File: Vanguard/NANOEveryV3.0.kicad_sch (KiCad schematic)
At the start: 57 parts, among them IC1 MPM3610, J1 -, J2 DNP, Q1 BSS138PS, Q2 BSS138PS, U1 ATMEGA4809, U2 AP2112K-3.3, U3 ATSAMD11D14A, U4 ICM-20602, U5 LM34DM_NOPB

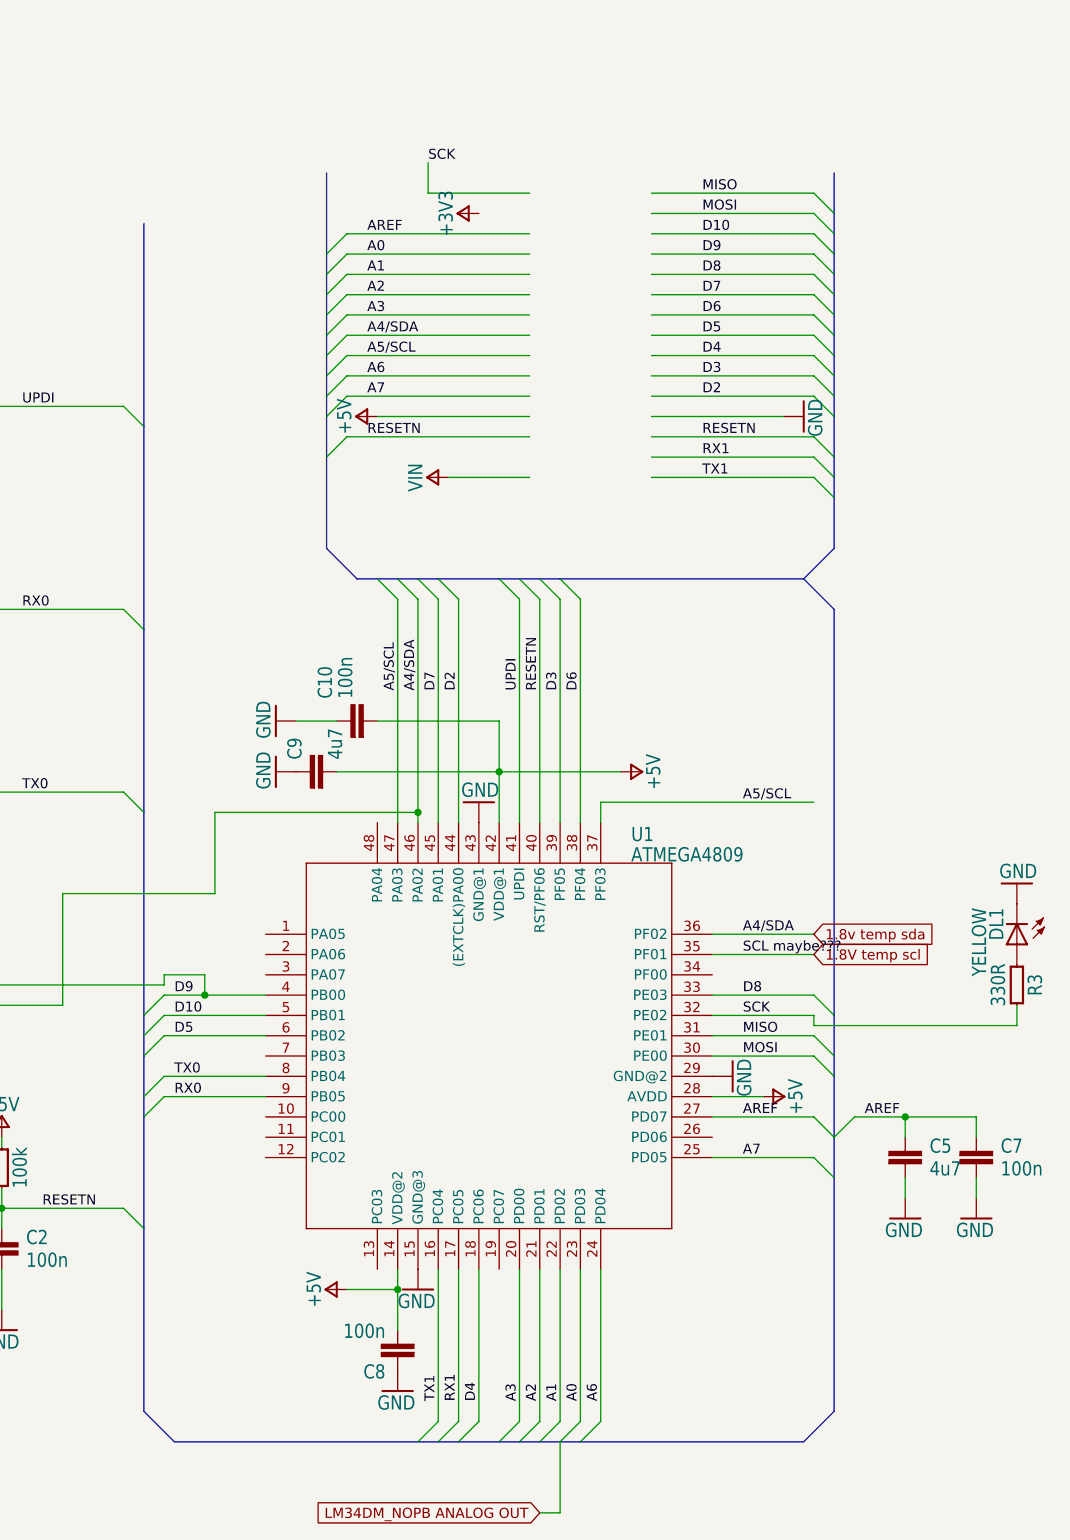
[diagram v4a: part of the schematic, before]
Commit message: removed headers + added mcu
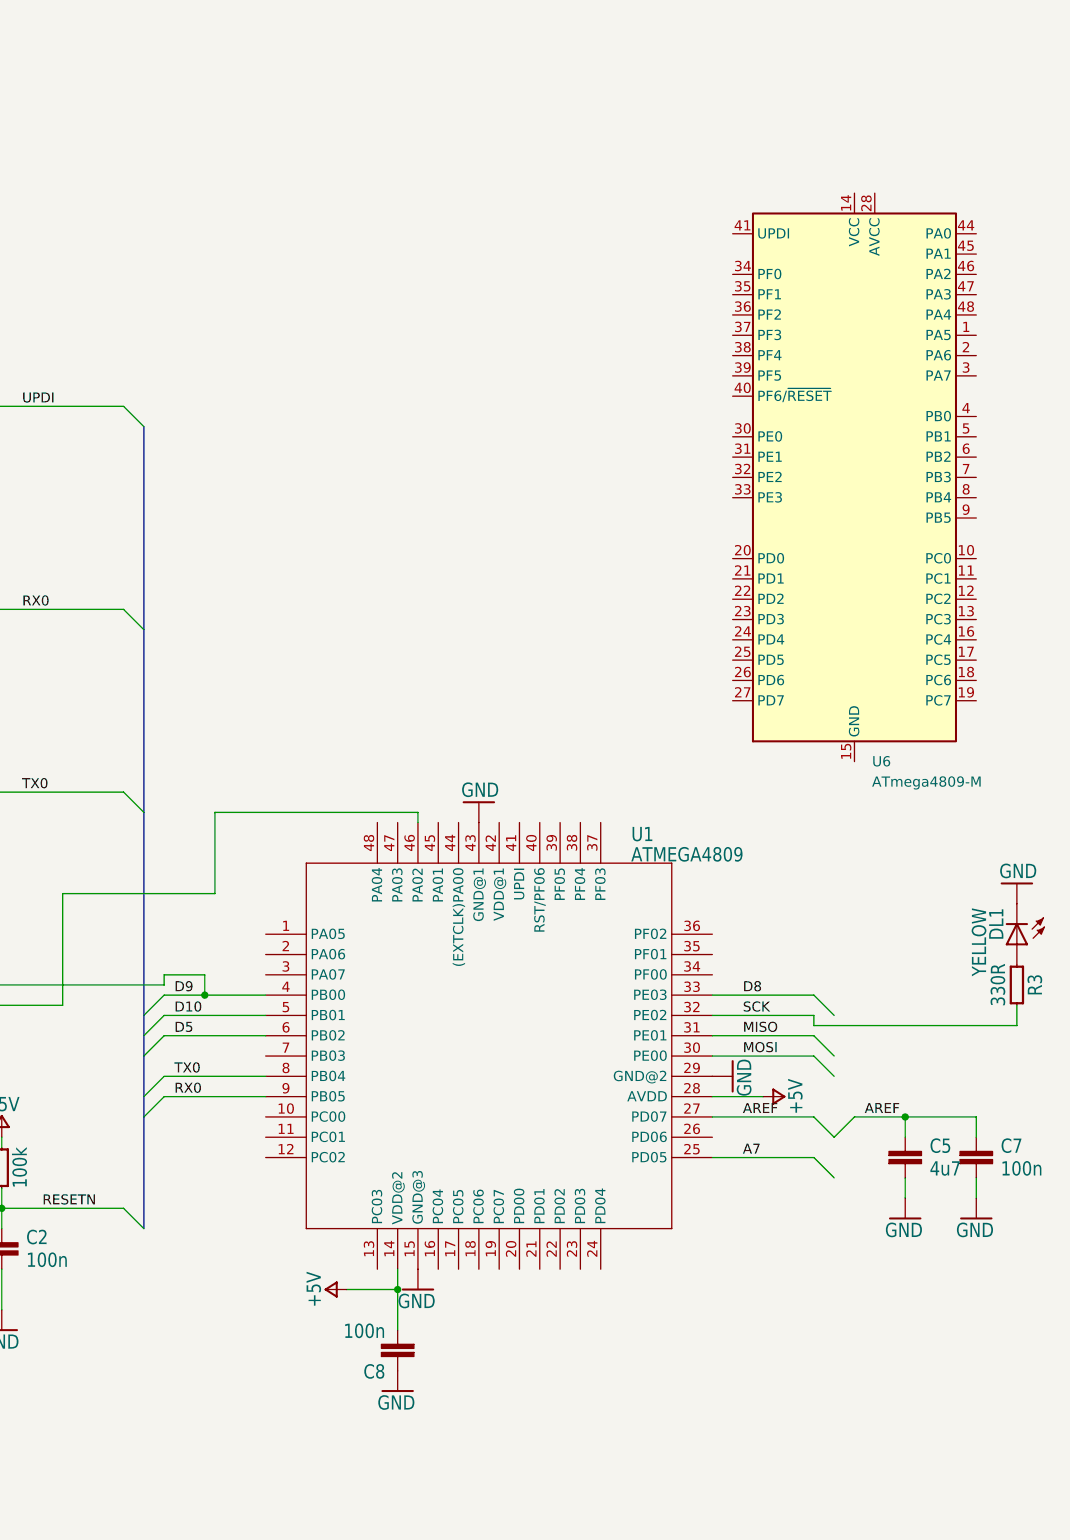
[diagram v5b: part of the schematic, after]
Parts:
- removed C10: 100n, Capacitor_SMD:C_0402_1005Metric, symbol NANOEveryV3.0-eagle-import:C-0402
- removed C9: 4u7, Capacitor_SMD:C_0402_1005Metric, symbol NANOEveryV3.0-eagle-import:C-0402
- added U6: ATmega4809-M, Package_DFN_QFN:UQFN-48-1EP_6x6mm_P0.4mm_EP4.62x4.62mm, symbol MCU_Microchip_ATmega:ATmega4809-M
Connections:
- net +5V: no longer U1.42 (VDD@1)
- net RESETN: no longer U1.40 (RST/PF06)
- net UPDI: no longer U1.41 (UPDI)
- net 1.8V temp scl: no longer names the net of U1.35 (PF01)
- net 1.8v temp sda: no longer names the net of U1.46 (PA02), U4.3 (SDA/SDI)
- net 1.8v temp sda: no longer U1.36 (PF02)
- net A0: no longer names the net of U1.23 (PD03)
- net A1: no longer names the net of U1.22 (PD02)
- net A2: no longer names the net of U1.21 (PD01)
- net A3: no longer names the net of U1.20 (PD00)
- net A5/SCL: no longer names the net of U1.37 (PF03)
- net A5/SCL: no longer U1.47 (PA03)
- net A6: no longer names the net of U1.24 (PD04)
- net D2: no longer names the net of U1.44 ((EXTCLK)PA00)
- net D3~{}: no longer names the net of U1.39 (PF05)
- net D4: no longer names the net of U1.18 (PC06)
- net D6~{}: no longer names the net of U1.38 (PF04)
- net D7: no longer names the net of U1.45 (PA01)
- net RX1: no longer names the net of U1.17 (PC05)
- net TX1: no longer names the net of U1.16 (PC04)
- new net: U6.14 (VCC), U6.42 (VCC)
- new net: U6.15 (GND), U6.29 (GND), U6.43 (GND), U6.49 (GND)

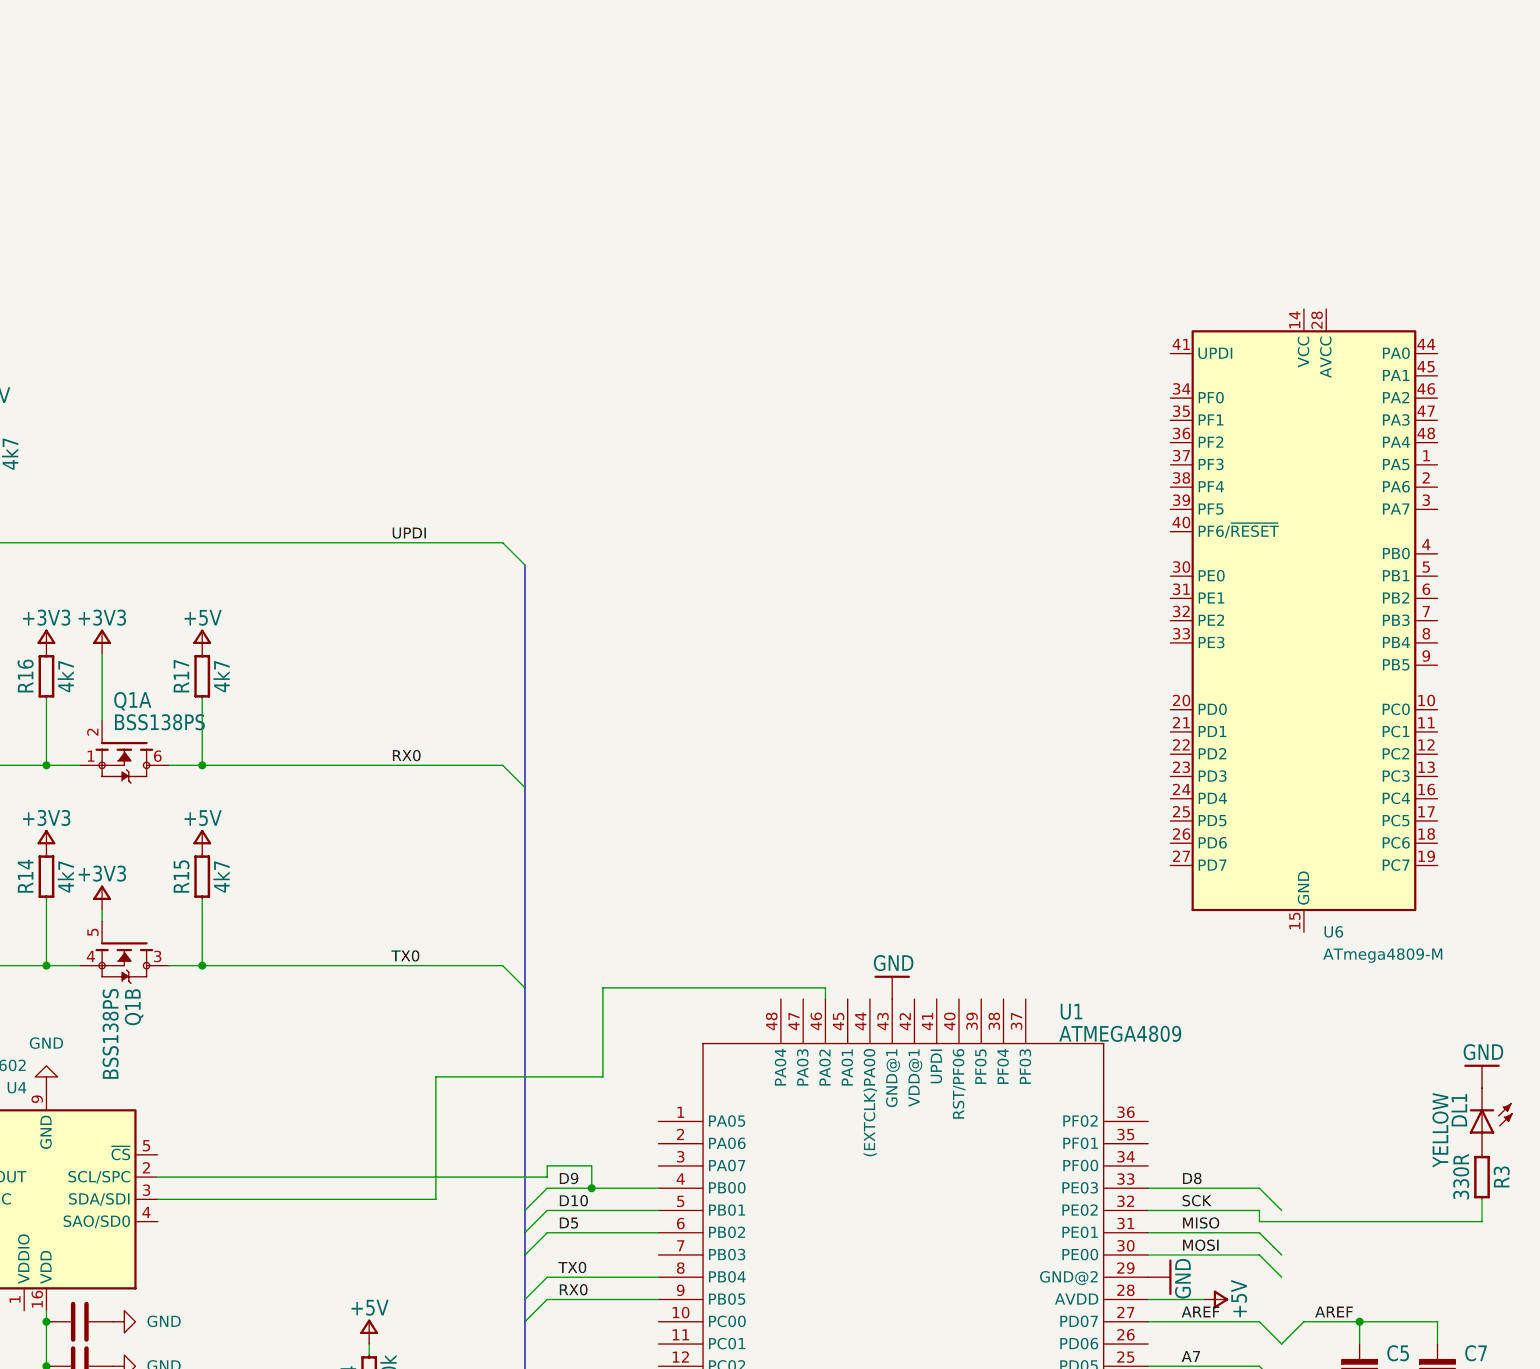
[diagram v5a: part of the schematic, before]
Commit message: New atmega chip added basic rewiring
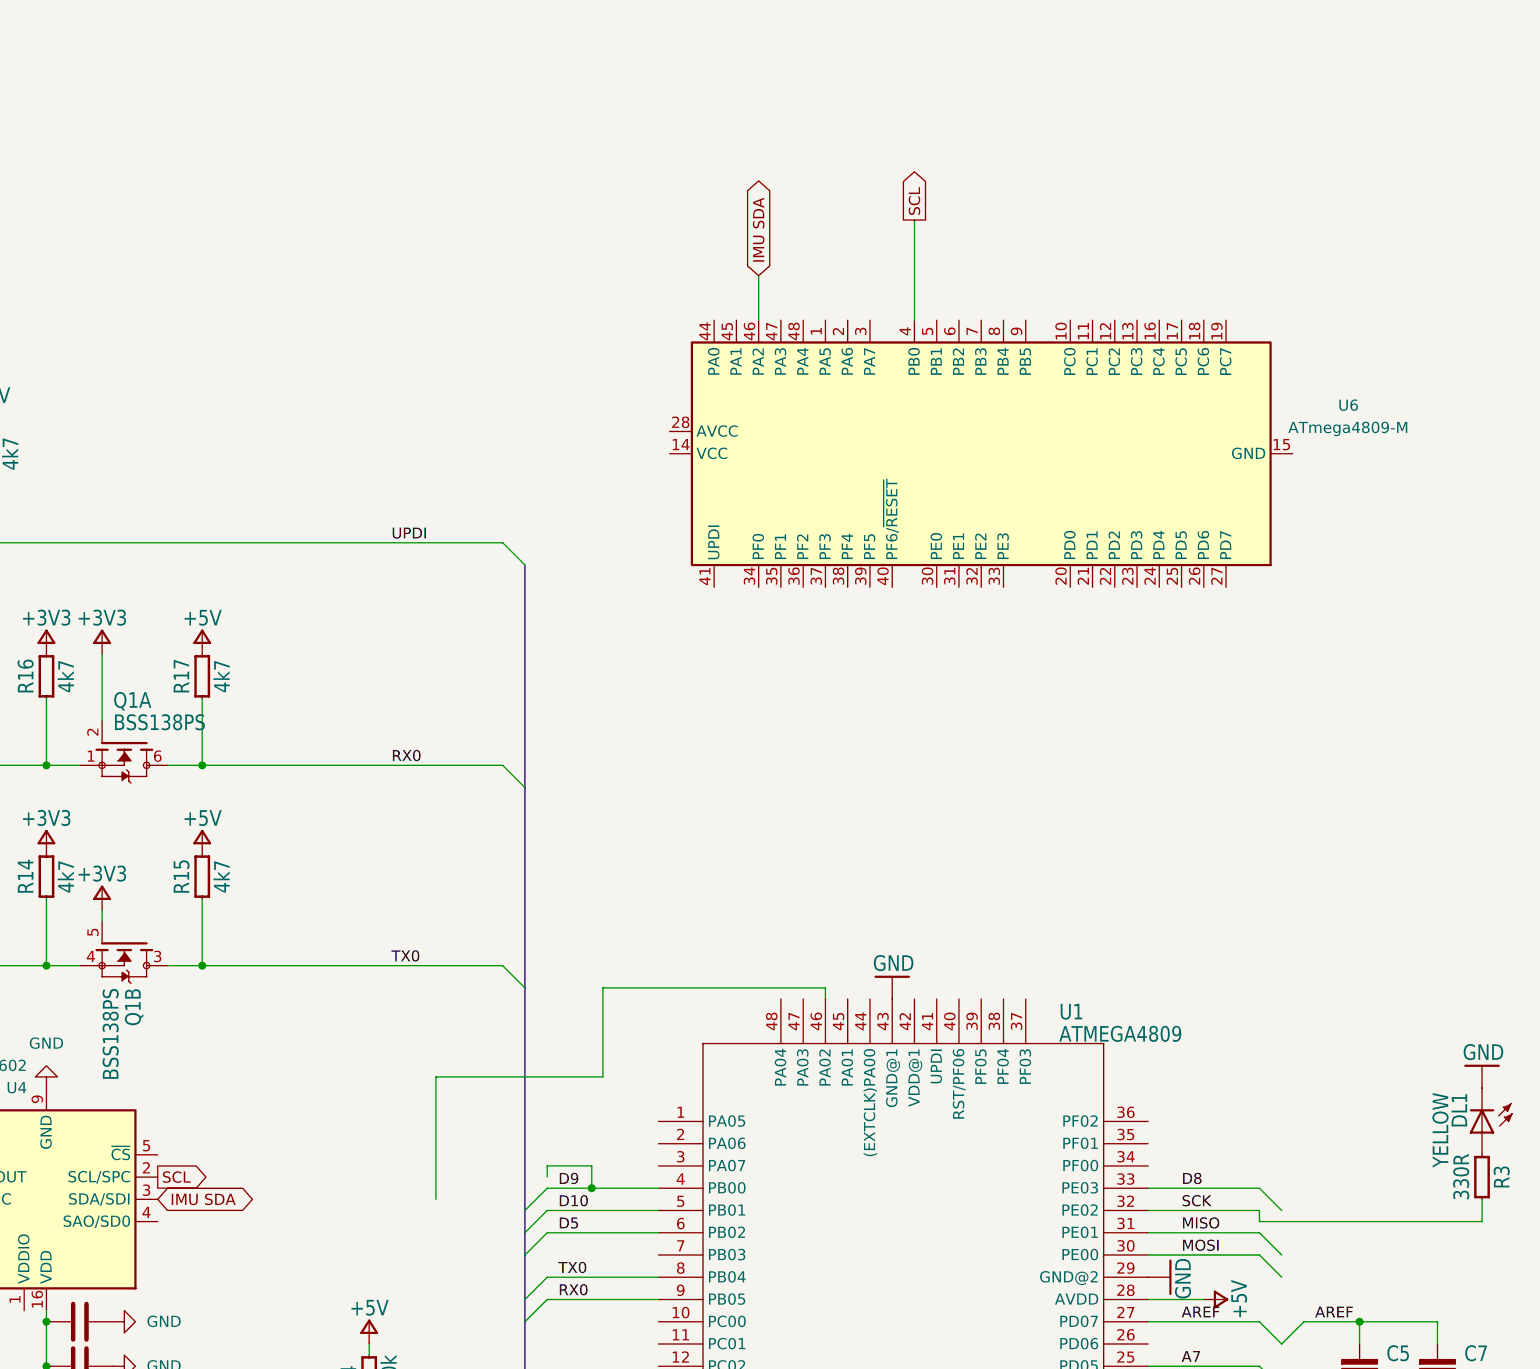
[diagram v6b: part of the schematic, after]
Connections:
- net D9~{}: no longer U4.2 (SCL/SPC)
- net at U1.46 (PA02): no longer U4.3 (SDA/SDI)
- net SCL: now reaches U6.4 (PB0)
- net SCL: now also U4.2 (SCL/SPC)
- net IMU SDA: now reaches U6.46 (PA2)
- net IMU SDA: now also U4.3 (SDA/SDI)
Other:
- moved on the sheet: U6
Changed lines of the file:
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@@
 	(wire
 		(pts
+			(xy 311.15 71.12) (xy 311.15 82.55)
+		)
+		(stroke
+			(width 0)
+			(type default)
+		)
+	)
+	(wire
+		(pts
 			(xy 73.66 50.8) (xy 73.66 52.07)
 		)
@@
 	(wire
 		(pts
-			(xy 111.76 50.8) (xy 111.76 49.53)
+			(xy 293.37 77.47) (xy 293.37 82.55)
 		)
 		(stroke
-			(width 0.1524)
-			(type solid)
+			(width 0)
+			(type default)
 		)
 	)
 	(wire
 		(pts
-			(xy 138.43 135.89) (xy 166.37 135.89)
+			(xy 111.76 50.8) (xy 111.76 49.53)
 		)
 		(stroke
@@
 	(wire
 		(pts
-			(xy 194.31 114.3) (xy 187.96 114.3)
+			(xy 138.43 135.89) (xy 166.37 135.89)
 		)
 		(stroke
@@
 	(wire
 		(pts
-			(xy 224.79 182.88) (xy 256.54 182.88)
+			(xy 194.31 114.3) (xy 187.96 114.3)
 		)
 		(stroke
-			(width 0)
-			(type default)
+			(width 0.1524)
+			(type solid)
 		)
 	)
@@
 	(wire
 		(pts
-			(xy 224.79 180.34) (xy 269.24 180.34)
-		)
-		(stroke
-			(width 0)
-			(type default)
-		)
-	)
-	(wire
-		(pts
 			(xy 186.69 123.19) (xy 186.69 125.73)
 		)
@@
 		)
 	)
+	(global_label "SCL"
+		(shape output)
+		(at 311.15 71.12 90)
+		(fields_autoplaced yes)
+		(effects
+			(font
+				(size 1.27 1.27)
+			)
+			(justify left)
+		)
+		(property "Intersheetrefs" "${INTERSHEET_REFS}"
+			(at 311.15 64.6272 90)
+			(effects
+				(font
+					(size 1.27 1.27)
+				)
+				(justify left)
+				(hide yes)
+			)
+		)
+	)
+	(global_label "IMU SDA"
+		(shape bidirectional)
+		(at 293.37 77.47 90)
+		(fields_autoplaced yes)
+		(effects
+			(font
+				(size 1.27 1.27)
+			)
+			(justify left)
+		)
+		(property "Intersheetrefs" "${INTERSHEET_REFS}"
+			(at 293.37 65.4511 90)
+			(effects
+				(font
+					(size 1.27 1.27)
+				)
+				(justify left)
+				(hide yes)
+			)
+		)
+	)
+	(global_label "SCL"
+		(shape output)
+		(at 224.79 180.34 0)
+		(fields_autoplaced yes)
+		(effects
+			(font
+				(size 1.27 1.27)
+			)
+			(justify left)
+		)
+		(property "Intersheetrefs" "${INTERSHEET_REFS}"
+			(at 231.2828 180.34 0)
+			(effects
+				(font
+					(size 1.27 1.27)
+				)
+				(justify left)
+				(hide yes)
+			)
+		)
+	)
 	(global_label "LM34DM_NOPB ANALOG OUT"
 		(shape input)
@@
 		)
 	)
+	(global_label "IMU SDA"
+		(shape bidirectional)
+		(at 224.79 182.88 0)
+		(fields_autoplaced yes)
+		(effects
+			(font
+				(size 1.27 1.27)
+			)
+			(justify left)
+		)
+		(property "Intersheetrefs" "${INTERSHEET_REFS}"
+			(at 236.8089 182.88 0)
+			(effects
+				(font
+					(size 1.27 1.27)
+				)
+				(justify left)
+				(hide yes)
+			)
+		)
+	)
 	(symbol
 		(lib_id "NANOEveryV3.0-eagle-import:Arduino-supply_GND")
@@
 	(symbol
 		(lib_id "MCU_Microchip_ATmega:ATmega4809-M")
-		(at 355.6 116.84 0)
+		(at 318.77 97.79 90)
 		(unit 1)
 		(exclude_from_sim no)
@@
 		(fields_autoplaced yes)
 		(property "Reference" "U6"
-			(at 357.7941 152.4 0)
+			(at 360.68 92.2938 90)
 			(effects
 				(font
 					(size 1.27 1.27)
 				)
-				(justify left)
 			)
 		)
 		(property "Value" "ATmega4809-M"
-			(at 357.7941 154.94 0)
+			(at 360.68 94.8338 90)
 			(effects
 				(font
 					(size 1.27 1.27)
 				)
-				(justify left)
 			)
 		)
 		(property "Footprint" "Package_DFN_QFN:UQFN-48-1EP_6x6mm_P0.4mm_EP4.62x4.62mm"
-			(at 355.6 116.84 0)
+			(at 318.77 97.79 0)
 			(effects
 				(font
@@
 		)
 		(property "Datasheet" "http://ww1.microchip.com/downloads/en/DeviceDoc/40002016A.pdf"
-			(at 355.6 116.84 0)
+			(at 318.77 97.79 0)
 			(effects
 				(font
@@
 		)
 		(property "Description" "20MHz, 48kB Flash, 6kB SRAM, 256B EEPROM, UQFN-48"
-			(at 355.6 116.84 0)
+			(at 318.77 97.79 0)
 			(effects
 				(font
